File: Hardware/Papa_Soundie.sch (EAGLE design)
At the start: 76 parts, among them J1 Audio Jack, J2 MICRO-SD_CARD_SOCKET, U1 ATMEGA328P_TQFP, U2 VS1000D, U3 3.3V, U4 4MB Flash, Y1 12MHz, Y2 8MHz

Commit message: final layout
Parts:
- J6: device SparkFun-Connectors:CONN_07 -> SparkFun-Connectors:CONN_05
- J8: device SparkFun-Connectors:CONN_04 -> SparkFun-Connectors:CONN_02
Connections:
- removed net A2: J8.3, U1.PC2(ADC2)
- removed net A3: J8.4, U1.PC3(ADC3)
- removed net D7: J6.7, U1.PD7(AIN1)
- removed net D8: J6.6, U1.PB0(ICP)
- net USBN: now also J10.2; no longer J10.1
- net USBP: now also J10.1; no longer J10.2
- net VS_RX: now also J11.2; no longer J11.1
- net VS_TX: now also J11.1; no longer J11.2
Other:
- note added: "Arduino Connectors"
- note added: "SPI Flash"
- note added: "VS1000D"
- note added: "VS1000D Connectors"
- note added: "v02"
- note removed: "Headers & Connectors"
- moved on the sheet: C10, C11, C12, C13, C14, C15, C3, C4, C5, C6, C7, C9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

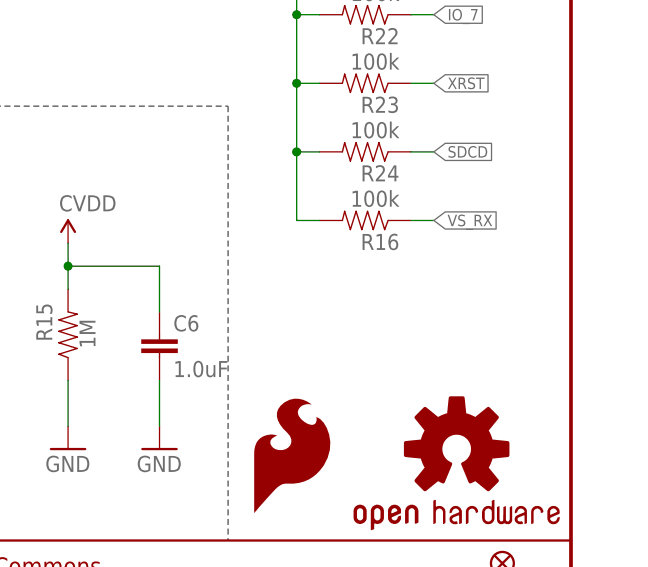
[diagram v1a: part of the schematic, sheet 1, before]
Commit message: added pull-up resistor on XCS line
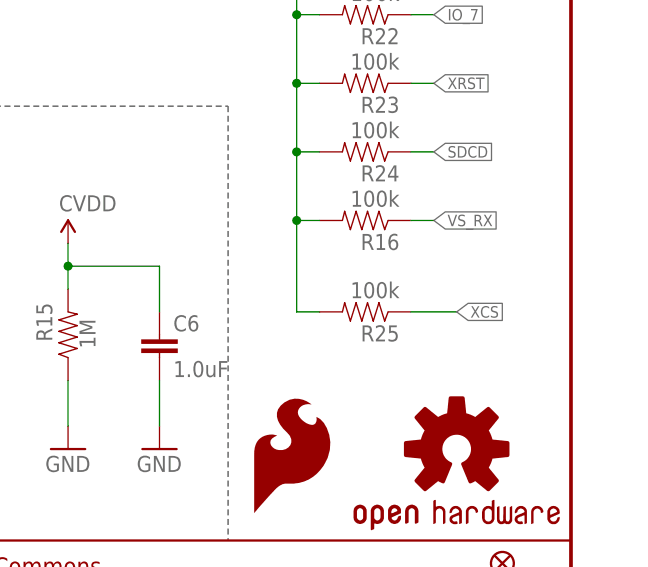
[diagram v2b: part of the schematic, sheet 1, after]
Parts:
- added R25: 100k, SparkFun-Resistors:100KOHM-1/10W-1%(0603)
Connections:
- net DVDD: now also R25.2
- net XCS: now also R25.1
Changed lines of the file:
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@@
 <part name="GND15" library="SparkFun-PowerSymbols" deviceset="GND" device=""/>
 <part name="J10" library="SparkFun-Connectors" deviceset="CONN_02" device=""/>
+<part name="R25" library="SparkFun-Resistors" deviceset="100KOHM-1/10W-1%(0603)" device="" value="100k"/>
 </parts>
 <sheets>
@@
 <instance part="GND20" gate="1" x="88.9" y="15.494"/>
 <instance part="SUPPLY11" gate="G$1" x="132.08" y="38.1"/>
+<instance part="R25" gate="G$1" x="226.06" y="60.96" rot="R180"/>
 </instances>
 <busses>
@@
 <wire x1="220.98" y1="71.12" x2="218.44" y2="71.12" width="0.1524" layer="91"/>
 <junction x="218.44" y="78.74"/>
+<wire x1="218.44" y1="71.12" x2="218.44" y2="60.96" width="0.1524" layer="91"/>
+<pinref part="R25" gate="G$1" pin="2"/>
+<wire x1="218.44" y1="60.96" x2="220.98" y2="60.96" width="0.1524" layer="91"/>
+<junction x="218.44" y="71.12"/>
 </segment>
 </net>
@@
 <label x="88.9" y="30.48" size="1.27" layer="95" rot="R180" xref="yes"/>
 </segment>
-</net>
+<segment>
+<pinref part="R25" gate="G$1" pin="1"/>
+<wire x1="231.14" y1="60.96" x2="236.22" y2="60.96" width="0.1524" layer="91"/>
+<label x="236.22" y="60.96" size="1.27" layer="95" xref="yes"/>
+</segment>
+</net>

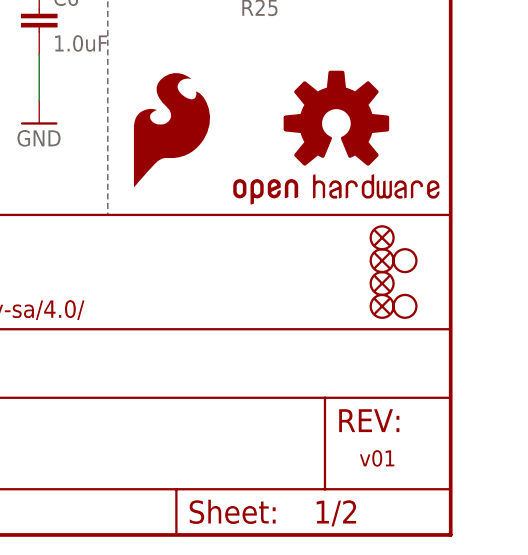
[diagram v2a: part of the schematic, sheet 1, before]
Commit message: added measurement to third standoff
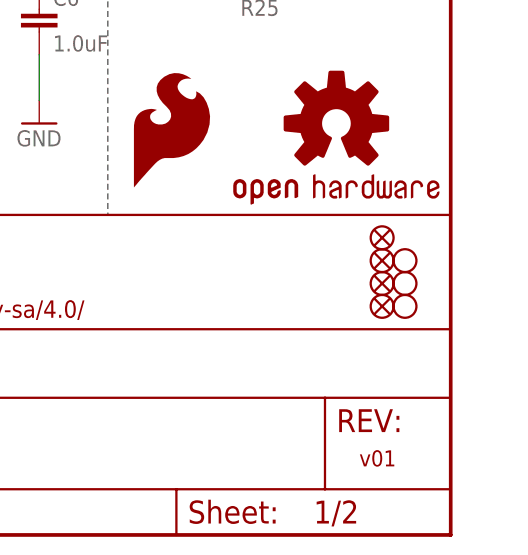
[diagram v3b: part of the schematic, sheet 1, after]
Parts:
- added H3: STAND-OFFTIGHT, SparkFun-Electromechanical:STAND-OFFTIGHT
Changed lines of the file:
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@@
 <part name="J10" library="SparkFun-Connectors" deviceset="CONN_02" device=""/>
 <part name="R25" library="SparkFun-Resistors" deviceset="100KOHM-1/10W-1%(0603)" device="" value="100k"/>
+<part name="H3" library="SparkFun-Electromechanical" deviceset="STAND-OFF" device="TIGHT"/>
 </parts>
 <sheets>
@@
 <instance part="SUPPLY11" gate="G$1" x="132.08" y="38.1"/>
 <instance part="R25" gate="G$1" x="226.06" y="60.96" rot="R180"/>
+<instance part="H3" gate="G$1" x="243.84" y="27.94"/>
 </instances>
 <busses>

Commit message: changes per QC Review
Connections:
- net AVDD: now also C4.1
- net VCC: no longer C4.1
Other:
- note removed: "v01"
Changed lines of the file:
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@@
 <plain>
 <text x="166.37" y="11.684" size="2.1844" layer="94" font="vector">Mary West</text>
-<text x="238.76" y="7.62" size="1.778" layer="94" font="vector">v01</text>
+<text x="238.76" y="7.62" size="1.778" layer="94" font="vector">v02</text>
 <wire x1="0" y1="60.96" x2="0" y2="63.5" width="0.1524" layer="97" style="shortdash"/>
 <text x="148.844" y="78.486" size="2.54" layer="97" font="vector" ratio="10">Decoupling</text>
@@
 </segment>
 <segment>
-<pinref part="C4" gate="G$1" pin="1"/>
-<pinref part="AVDD6" gate="G$1" pin="VCC"/>
-<wire x1="175.26" y1="68.58" x2="175.26" y2="60.96" width="0.1524" layer="91"/>
-</segment>
-<segment>
 <pinref part="U4" gate="G$1" pin="VCC"/>
 <wire x1="127" y1="30.48" x2="132.08" y2="30.48" width="0.1524" layer="91"/>
@@
 <junction x="81.28" y="170.18"/>
 </segment>
-</net>
+<segment>
+<pinref part="C4" gate="G$1" pin="1"/>
+<pinref part="AVDD6" gate="G$1" pin="VCC"/>
+<wire x1="175.26" y1="68.58" x2="175.26" y2="60.96" width="0.1524" layer="91"/>
+</segment>
+</net>

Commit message: Updated design for rev 2
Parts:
- removed C27: 1.0uF, SparkFun-Capacitors:1.0UF-0603-16V-10%
- removed R32: 39k, SparkFun-Resistors:39KOHM-0603-1/10W-1%
- added D2, D3: RED, SparkFun-LED:LED-RED0603
- added J12: (no value), SparkFun-Connectors:CONN_01
- added R26: 2.0k, SparkFun-Resistors:2.0KOHM-0603-1/10W-5%
- R18: value 68.1k -> 2.0k; device SparkFun-Resistors:68.1KOHM-0603-1/10W-1% -> SparkFun-Resistors:2.0KOHM-0603-1/10W-5%
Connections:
- removed net N$60: C27.2, R32.2
- new net N$34: D2.C, R18.2
- new net N$35: D2.A, U2.NFDIO5/IO0_5
- new net N$36: D3.C, R26.2
- new net RST: C8.2, J12.1, R9.1, S1.2, U1.PC6(/RESET)
- net GND: now also C3.2, J2.CD2, R26.1
- net N$31: now also D3.A, U1.PC2(ADC2); no longer C8.2, R9.1, S1.2, U1.PC6(/RESET)
- net PWRBTN: now also U1.PD7(AIN1); no longer R18.2, R32.1
- net RAW: no longer C27.1
- net SD3V3: no longer C3.2
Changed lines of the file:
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@@
 <?xml version="1.0" encoding="utf-8"?>
 <!DOCTYPE eagle SYSTEM "eagle.dtd">
-<eagle version="7.7.0">
+<eagle version="8.5.1">
 <drawing>
 <settings>
 <setting alwaysvectorfont="no"/>
+<setting keepoldvectorfont="yes"/>
 <setting verticaltext="up"/>
 </settings>
@@
 <part name="GND10" library="SparkFun-PowerSymbols" deviceset="GND" device=""/>
 <part name="GND29" library="SparkFun-Aesthetics" deviceset="GND" device=""/>
-<part name="R18" library="SparkFun-Resistors" deviceset="68.1KOHM" device="-0603-1/10W-1%" value="68.1k"/>
-<part name="R32" library="SparkFun-Resistors" deviceset="39KOHM" device="-0603-1/10W-1%" value="39k"/>
-<part name="C27" library="SparkFun-Capacitors" deviceset="1.0UF" device="-0603-16V-10%" value="1.0uF"/>
-<part name="GND30" library="SparkFun-PowerSymbols" deviceset="GND" device=""/>
 <part name="J6" library="SparkFun-Connectors" deviceset="CONN_05" device=""/>
 <part name="J7" library="SparkFun-Connectors" deviceset="CONN_04" device=""/>
@@
 <part name="R25" library="SparkFun-Resistors" deviceset="100KOHM-1/10W-1%(0603)" device="" value="100k"/>
 <part name="H3" library="SparkFun-Electromechanical" deviceset="STAND-OFF" device="TIGHT"/>
+<part name="GND13" library="SparkFun-PowerSymbols" deviceset="GND" device=""/>
+<part name="GND21" library="SparkFun-Aesthetics" deviceset="GND" device=""/>
+<part name="D2" library="SparkFun-LED" deviceset="LED-RED" device="0603" value="RED"/>
+<part name="R18" library="SparkFun-Resistors" deviceset="2.0KOHM" device="-0603-1/10W-5%" value="2.0k"/>
+<part name="GND23" library="SparkFun-Aesthetics" deviceset="GND" device=""/>
+<part name="R26" library="SparkFun-Resistors" deviceset="2.0KOHM" device="-0603-1/10W-5%" value="2.0k"/>
+<part name="D3" library="SparkFun-LED" deviceset="LED-RED" device="0603" value="RED"/>
+<part name="GND30" library="SparkFun-PowerSymbols" deviceset="GND" device=""/>
+<part name="J12" library="SparkFun-Connectors" deviceset="CONN_01" device=""/>
 </parts>
 <sheets>
@@
 <instance part="R25" gate="G$1" x="226.06" y="60.96" rot="R180"/>
 <instance part="H3" gate="G$1" x="243.84" y="27.94"/>
+<instance part="GND21" gate="1" x="48.26" y="12.7"/>
+<instance part="D2" gate="G$1" x="30.48" y="116.84"/>
+<instance part="R18" gate="G$1" x="30.48" y="104.14" rot="R90"/>
+<instance part="GND23" gate="1" x="30.48" y="93.98"/>
 </instances>
 <busses>
@@
 <pinref part="GND20" gate="1" pin="GND"/>
 <wire x1="88.9" y1="18.034" x2="88.9" y2="17.78" width="0.1524" layer="91"/>
+</segment>
+<segment>
+<pinref part="J2" gate="1" pin="CD2"/>
+<wire x1="45.72" y1="17.78" x2="48.26" y2="17.78" width="0.1524" layer="91"/>
+<wire x1="48.26" y1="17.78" x2="48.26" y2="15.24" width="0.1524" layer="91"/>
+<pinref part="GND21" gate="1" pin="GND"/>
+</segment>
+<segment>
+<pinref part="R18" gate="G$1" pin="1"/>
+<pinref part="GND23" gate="1" pin="GND"/>
+<wire x1="30.48" y1="99.06" x2="30.48" y2="96.52" width="0.1524" layer="91"/>
 </segment>
 </net>
@@
 <wire x1="109.22" y1="101.6" x2="111.76" y2="101.6" width="0.1524" layer="91"/>
 <label x="111.76" y="101.6" size="1.27" layer="95" xref="yes"/>
+</segment>
+</net>
+<net name="N$34" class="0">
+<segment>
+<pinref part="D2" gate="G$1" pin="C"/>
+<pinref part="R18" gate="G$1" pin="2"/>
+<wire x1="30.48" y1="111.76" x2="30.48" y2="109.22" width="0.1524" layer="91"/>
+</segment>
+</net>
+<net name="N$35" class="0">
+<segment>
+<pinref part="U2" gate="G$1" pin="NFDIO5/IO0_5"/>
+<wire x1="53.34" y1="121.92" x2="30.48" y2="121.92" width="0.1524" layer="91"/>
+<pinref part="D2" gate="G$1" pin="A"/>
+<wire x1="30.48" y1="121.92" x2="30.48" y2="119.38" width="0.1524" layer="91"/>
 </segment>
 </net>
@@
 <instance part="C14" gate="G$1" x="200.66" y="152.4"/>
 <instance part="GND10" gate="1" x="200.66" y="144.78"/>
-<instance part="R18" gate="&gt;NAME" x="228.6" y="137.16" smashed="yes" rot="R90">
-<attribute name="NAME" x="227.076" y="137.16" size="1.778" layer="95" font="vector" rot="R90" align="bottom-center"/>
-<attribute name="VALUE" x="230.124" y="137.16" size="1.778" layer="96" font="vector" rot="R90" align="top-center"/>
-</instance>
-<instance part="R32" gate="G$1" x="228.6" y="152.4" rot="R90"/>
-<instance part="C27" gate="G$1" x="228.6" y="165.1"/>
-<instance part="GND30" gate="1" x="228.6" y="124.46"/>
 <instance part="J6" gate="G$1" x="53.34" y="38.1"/>
 <instance part="J7" gate="G$1" x="93.98" y="20.32"/>
@@
 <instance part="GND15" gate="1" x="104.14" y="48.26"/>
 <instance part="J10" gate="G$1" x="185.42" y="71.12"/>
+<instance part="GND13" gate="1" x="149.86" y="144.78"/>
+<instance part="R26" gate="G$1" x="121.92" y="137.16" rot="R90"/>
+<instance part="D3" gate="G$1" x="121.92" y="149.86"/>
+<instance part="GND30" gate="1" x="121.92" y="127"/>
+<instance part="J12" gate="G$1" x="91.44" y="12.7"/>
 </instances>
 <busses>
@@
 </segment>
 <segment>
-<pinref part="R18" gate="&gt;NAME" pin="1"/>
-<wire x1="228.6" y1="132.08" x2="228.6" y2="127" width="0.1524" layer="91"/>
-<pinref part="GND30" gate="1" pin="GND"/>
-</segment>
-<segment>
 <pinref part="J7" gate="G$1" pin="4"/>
 <wire x1="99.06" y1="25.4" x2="116.84" y2="25.4" width="0.1524" layer="91"/>
@@
 <wire x1="104.14" y1="50.8" x2="104.14" y2="48.26" width="0.1524" layer="91"/>
 </segment>
-</net>
-<net name="N$31" class="0">
+<segment>
+<pinref part="C3" gate="G$1" pin="2"/>
+<wire x1="149.86" y1="149.86" x2="149.86" y2="147.32" width="0.1524" layer="91"/>
+<pinref part="GND13" gate="1" pin="GND"/>
+</segment>
+<segment>
+<pinref part="R26" gate="G$1" pin="1"/>
+<pinref part="GND30" gate="1" pin="GND"/>
+<wire x1="121.92" y1="129.54" x2="121.92" y2="132.08" width="0.1524" layer="91"/>
+</segment>
+</net>
+<net name="RST" class="0">
 <segment>
 <pinref part="U1" gate="U$1" pin="PC6(/RESET)"/>
@@
 <pinref part="C8" gate="G$1" pin="2"/>
 <pinref part="S1" gate="G$1" pin="2"/>
-<wire x1="40.64" y1="160.02" x2="25.4" y2="160.02" width="0.1524" layer="91"/>
+<wire x1="40.64" y1="160.02" x2="30.48" y2="160.02" width="0.1524" layer="91"/>
+<wire x1="30.48" y1="160.02" x2="25.4" y2="160.02" width="0.1524" layer="91"/>
 <wire x1="25.4" y1="160.02" x2="22.86" y2="160.02" width="0.1524" layer="91"/>
 <wire x1="25.4" y1="157.48" x2="25.4" y2="160.02" width="0.1524" layer="91"/>
@@
 <wire x1="40.64" y1="165.1" x2="40.64" y2="160.02" width="0.1524" layer="91"/>
 <junction x="40.64" y="160.02"/>
+<wire x1="30.48" y1="160.02" x2="30.48" y2="165.1" width="0.1524" layer="91"/>
+<wire x1="30.48" y1="165.1" x2="33.02" y2="165.1" width="0.1524" layer="91"/>
+<label x="33.02" y="165.1" size="1.27" layer="95" xref="yes"/>
+</segment>
+<segment>
+<pinref part="J12" gate="G$1" pin="1"/>
+<wire x1="99.06" y1="12.7" x2="101.6" y2="12.7" width="0.1524" layer="91"/>
+<label x="101.6" y="12.7" size="1.27" layer="95" xref="yes"/>
 </segment>
 </net>
@@
 </segment>
 <segment>
-<pinref part="C27" gate="G$1" pin="1"/>
-<wire x1="228.6" y1="170.18" x2="228.6" y2="172.72" width="0.1524" layer="91"/>
-<wire x1="228.6" y1="172.72" x2="223.52" y2="172.72" width="0.1524" layer="91"/>
-<label x="223.52" y="172.72" size="1.27" layer="95" font="vector" rot="R180" xref="yes"/>
-</segment>
-<segment>
 <pinref part="J4" gate="G$1" pin="VCC"/>
 <wire x1="22.86" y1="40.64" x2="27.94" y2="40.64" width="0.1524" layer="91"/>
@@
 <segment>
 <pinref part="U3" gate="G$1" pin="EN"/>
-<wire x1="175.26" y1="154.94" x2="170.18" y2="154.94" width="0.1524" layer="91"/>
+<wire x1="175.26" y1="154.94" x2="167.64" y2="154.94" width="0.1524" layer="91"/>
 <label x="167.64" y="154.94" size="1.27" layer="95" font="vector" rot="R180" xref="yes"/>
-<pinref part="C3" gate="G$1" pin="2"/>
-<wire x1="170.18" y1="154.94" x2="167.64" y2="154.94" width="0.1524" layer="91"/>
-<wire x1="149.86" y1="149.86" x2="149.86" y2="147.32" width="0.1524" layer="91"/>
-<wire x1="149.86" y1="147.32" x2="165.1" y2="147.32" width="0.1524" layer="91"/>
-<wire x1="165.1" y1="147.32" x2="165.1" y2="152.4" width="0.1524" layer="91"/>
-<wire x1="165.1" y1="152.4" x2="170.18" y2="152.4" width="0.1524" layer="91"/>
-<wire x1="170.18" y1="152.4" x2="170.18" y2="154.94" width="0.1524" layer="91"/>
-<junction x="170.18" y="154.94"/>
-</segment>
-</net>
-<net name="N$60" class="0">
-<segment>
-<pinref part="R32" gate="G$1" pin="2"/>
-<pinref part="C27" gate="G$1" pin="2"/>
-<wire x1="228.6" y1="157.48" x2="228.6" y2="162.56" width="0.1524" layer="91"/>
 </segment>
 </net>
 <net name="PWRBTN" class="0">
 <segment>
-<pinref part="R18" gate="&gt;NAME" pin="2"/>
-<pinref part="R32" gate="G$1" pin="1"/>
-<wire x1="228.6" y1="142.24" x2="228.6" y2="144.78" width="0.1524" layer="91"/>
-<wire x1="228.6" y1="144.78" x2="228.6" y2="147.32" width="0.1524" layer="91"/>
-<wire x1="228.6" y1="144.78" x2="223.52" y2="144.78" width="0.1524" layer="91"/>
-<junction x="228.6" y="144.78"/>
-<label x="223.52" y="144.78" size="1.27" layer="95" font="vector" rot="R180" xref="yes"/>
+<pinref part="U1" gate="U$1" pin="PD7(AIN1)"/>
+<wire x1="104.14" y1="119.38" x2="106.68" y2="119.38" width="0.1524" layer="91"/>
+<label x="106.68" y="119.38" size="1.27" layer="95" xref="yes"/>
 </segment>
 </net>
@@
 </segment>
 </net>
+<net name="N$31" class="0">
+<segment>
+<pinref part="U1" gate="U$1" pin="PC2(ADC2)"/>
+<wire x1="104.14" y1="154.94" x2="121.92" y2="154.94" width="0.1524" layer="91"/>
+<pinref part="D3" gate="G$1" pin="A"/>
+<wire x1="121.92" y1="154.94" x2="121.92" y2="152.4" width="0.1524" layer="91"/>
+</segment>
+</net>
+<net name="N$36" class="0">
+<segment>
+<pinref part="D3" gate="G$1" pin="C"/>
+<pinref part="R26" gate="G$1" pin="2"/>
+<wire x1="121.92" y1="144.78" x2="121.92" y2="142.24" width="0.1524" layer="91"/>
+</segment>
+</net>
